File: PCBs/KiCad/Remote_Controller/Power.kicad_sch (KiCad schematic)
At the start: 24 parts, among them Q101 IRFML8244TRPBF, Q102 IRFML8244TRPBF, SW101 Power Switch, U101 AP63203WU, U102 LM74700, U103 MCP1700T-3002E/TT, U104 LM74700

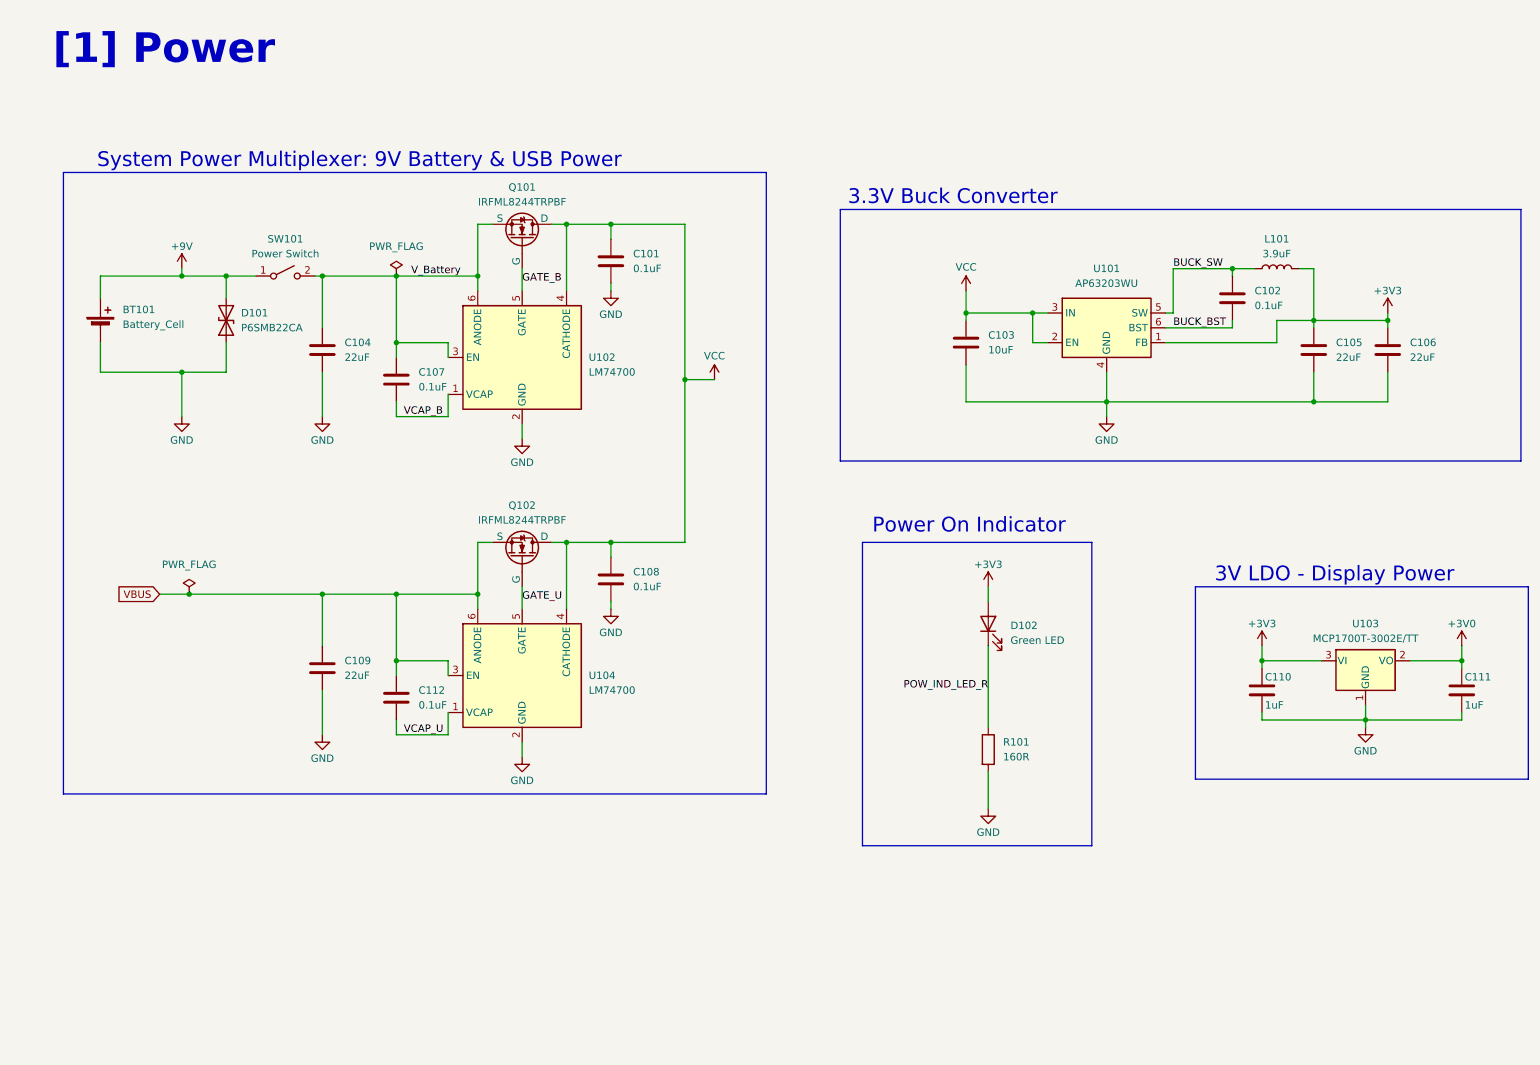
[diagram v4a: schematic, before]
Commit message: Add Latching Power On-Off switch circuit - allows user to turn device on and off with a tactile switch
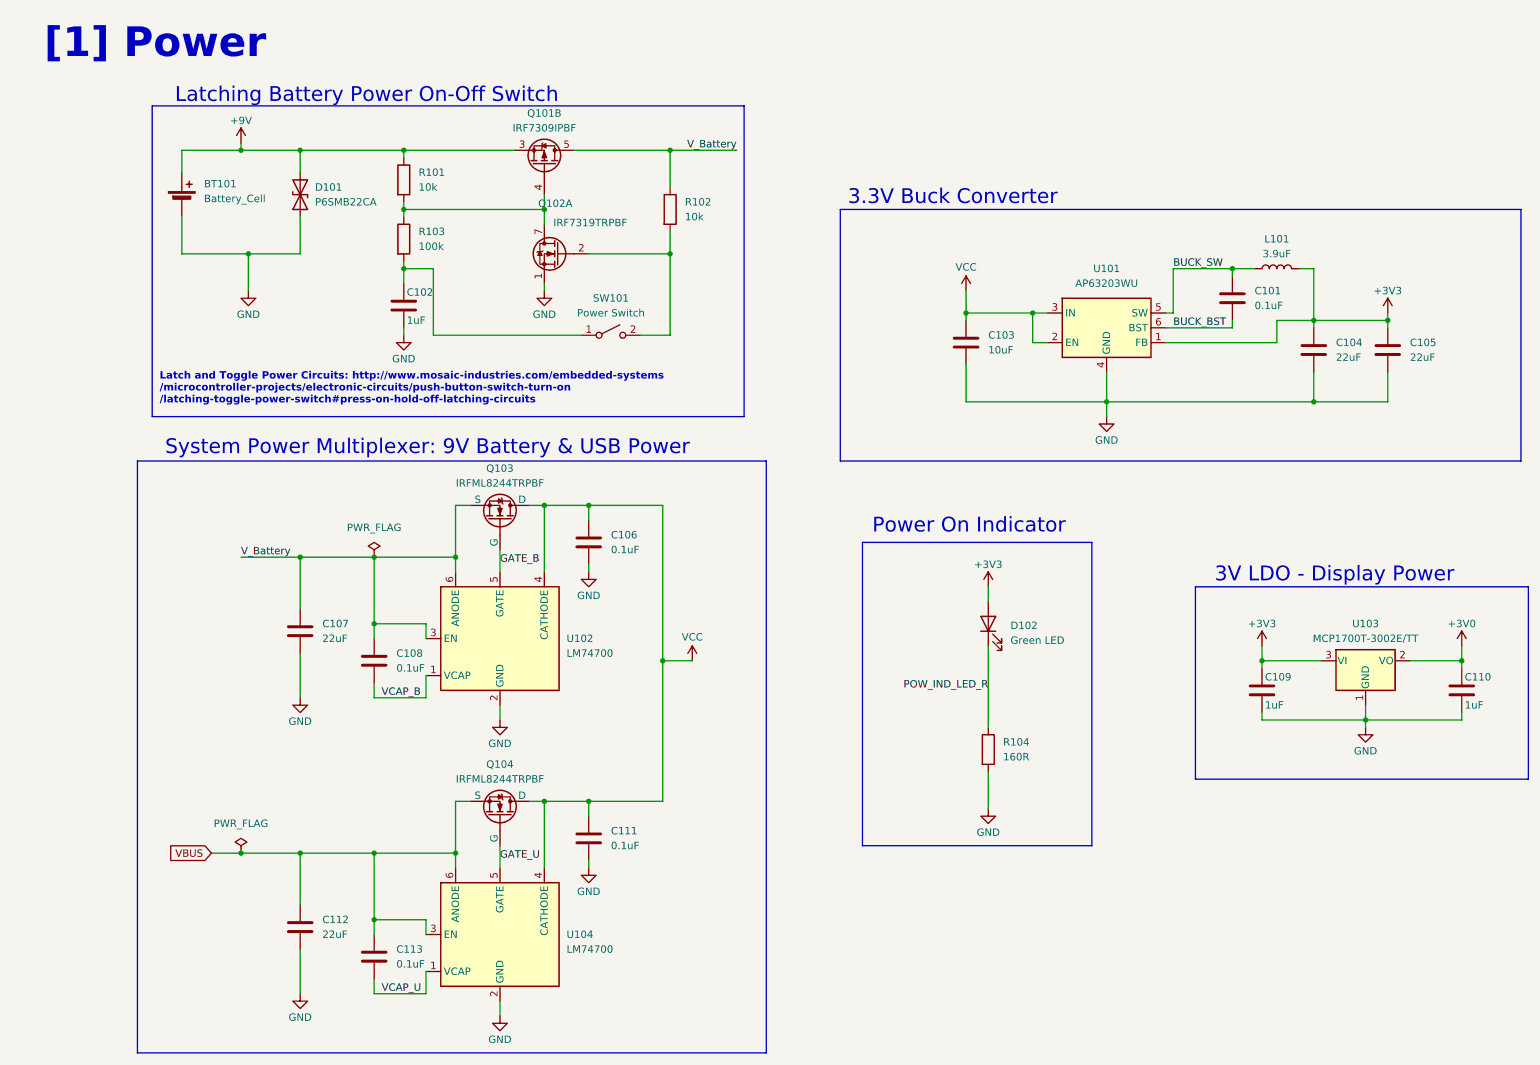
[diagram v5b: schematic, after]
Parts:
- added C102: 1uF, Capacitor_SMD:C_0402_1005Metric, symbol Device:C
- added Q101: IRF7309IPBF, Package_TO_SOT_THT:TO-220F-5_P3.4x2.06mm_StaggerEven_Lead1.86mm_Vertical, symbol Transistor_FET:IRF7309IPBF
- added Q102: IRF7319TRPBF, Package_TO_SOT_THT:TO-220F-5_P3.4x2.06mm_StaggerEven_Lead1.86mm_Vertical, symbol Transistor_FET:IRF7309IPBF
- added R101, R102: 10k, Resistor_SMD:R_0402_1005Metric, symbol Device:R
- added R103: 100k, Resistor_SMD:R_0603_1608Metric, symbol Device:R
- SW101: footprint (none) -> Button_Switch_SMD:SW_Push_1P1T_NO_CK_PTS125Sx43PSMTR
- renumbered C102 to C101, C105 to C104, C106 to C105, C101 to C106, C104 to C107, C107 to C108, C110 to C109, C111 to C110, C108 to C111, C109 to C112, C112 to C113, Q101 to Q103, Q102 to Q104, R101 to R104
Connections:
- net +9V: now also Q101.3 (1), R101.1; no longer SW101.1 (A)
- net GND: now also C102.2, Q102.1 (S)
- net V_Battery: now also Q101.5 (D), Q101.6 (D), R102.1; no longer SW101.2 (B)
- new net: Q102.2 (G), R102.2, SW101.2 (B)
- new net: C102.1, R103.2, SW101.1 (A)
- new net: Q101.4 (G), Q102.7 (D), Q102.8 (D), R101.2, R103.1
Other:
- note added: "Latch and Toggle Power Circuits: http://www.mosaic-industries.com/embedded-systems /microcontroller-projects/electronic-circuits/push-button-switch-turn-on /latching-toggle-power-switch#press-on-hold-off-latching-circuits"
- note added: "Latching Battery Power On-Off Switch"
- moved on the sheet: C106, C107, C108, C111, C112, C113, Q103, Q104, U102, U104

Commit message: Add Joystick footprint and passed ERC
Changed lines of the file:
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@@
 	)
 	(junction
+		(at 181.61 67.31)
+		(diameter 0)
+		(color 0 0 0 0)
+	)
+	(junction
 		(at 246.38 68.58)
 		(diameter 0)
@@
 	)
 	(junction
+		(at 64.77 39.37)
+		(diameter 0)
+		(color 0 0 0 0)
+	)
+	(junction
 		(at 198.12 82.55)
 		(diameter 0)
@@
 	(wire
 		(pts
-			(xy 59.69 39.37) (xy 77.47 39.37)
+			(xy 59.69 39.37) (xy 64.77 39.37)
 		)
 		(stroke
@@
 	(wire
 		(pts
+			(xy 181.61 67.31) (xy 173.99 67.31)
+		)
+		(stroke
+			(width 0)
+			(type default)
+		)
+	)
+	(wire
+		(pts
 			(xy 177.8 114.3) (xy 177.8 116.84)
 		)
@@
 	(wire
 		(pts
-			(xy 185.42 67.31) (xy 173.99 67.31)
+			(xy 185.42 67.31) (xy 181.61 67.31)
 		)
 		(stroke
@@
 	(wire
 		(pts
+			(xy 64.77 39.37) (xy 77.47 39.37)
+		)
+		(stroke
+			(width 0)
+			(type default)
+		)
+	)
+	(wire
+		(pts
 			(xy 259.08 135.89) (xy 259.08 137.16)
 		)
@@
 	(symbol
 		(lib_id "power:PWR_FLAG")
+		(at 181.61 67.31 0)
+		(unit 1)
+		(exclude_from_sim no)
+		(in_bom yes)
+		(on_board yes)
+		(dnp no)
+		(fields_autoplaced yes)
+		(property "Reference" "#FLG0104"
+			(at 181.61 65.405 0)
+			(effects
+				(font
+					(size 1.27 1.27)
+				)
+				(hide yes)
+			)
+		)
+		(property "Value" "PWR_FLAG"
+			(at 181.61 62.23 0)
+			(effects
+				(font
+					(size 1.27 1.27)
+				)
+			)
+		)
+		(property "Footprint" ""
+			(at 181.61 67.31 0)
+			(effects
+				(font
+					(size 1.27 1.27)
+				)
+				(hide yes)
+			)
+		)
+		(property "Datasheet" "~"
+			(at 181.61 67.31 0)
+			(effects
+				(font
+					(size 1.27 1.27)
+				)
+				(hide yes)
+			)
+		)
+		(property "Description" "Special symbol for telling ERC where power comes from"
+			(at 181.61 67.31 0)
+			(effects
+				(font
+					(size 1.27 1.27)
+				)
+				(hide yes)
+			)
+		)
+		(pin "1"
+		)
+		(instances
+			(project "Remote_Controller"
+				(path "/7afb5074-6b77-4607-a5eb-938c2def45ba/bc757f9b-317d-459c-8896-b31b23ed4983"
+					(reference "#FLG0104")
+					(unit 1)
+				)
+			)
+		)
+	)
+	(symbol
+		(lib_id "power:PWR_FLAG")
 		(at 72.39 109.22 0)
 		(unit 1)
@@
 					(unit 1)
 				)
+			)
+		)
+	)
+	(symbol
+		(lib_id "power:PWR_FLAG")
+		(at 64.77 39.37 0)
+		(unit 1)
+		(exclude_from_sim no)
+		(in_bom yes)
+		(on_board yes)
+		(dnp no)
+		(fields_autoplaced yes)
+		(property "Reference" "#FLG0103"
+			(at 64.77 37.465 0)
+			(effects
+				(font
+					(size 1.27 1.27)
+				)
+				(hide yes)
+			)
+		)
+		(property "Value" "PWR_FLAG"
+			(at 64.77 34.29 0)
+			(effects
+				(font
+					(size 1.27 1.27)
+				)
+			)
+		)
+		(property "Footprint" ""
+			(at 64.77 39.37 0)
+			(effects
+				(font
+					(size 1.27 1.27)
+				)
+				(hide yes)
+			)
+		)
+		(property "Datasheet" "~"
+			(at 64.77 39.37 0)
+			(effects
+				(font
+					(size 1.27 1.27)
+				)
+				(hide yes)
+			)
+		)
+		(property "Description" "Special symbol for telling ERC where power comes from"
+			(at 64.77 39.37 0)
+			(effects
+				(font
+					(size 1.27 1.27)
+				)
+				(hide yes)
+			)
+		)
+		(pin "1"
+		)
+		(instances
+			(project "Remote_Controller"
+				(path "/7afb5074-6b77-4607-a5eb-938c2def45ba/bc757f9b-317d-459c-8896-b31b23ed4983"
+					(reference "#FLG0103")
+					(unit 1)
+				)

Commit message: Updated joystick symbol, correct Dual fet footprint and annotated news in power toggle circuit
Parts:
- removed Q102: IRF7319TRPBF, Package_TO_SOT_THT:TO-220F-5_P3.4x2.06mm_StaggerEven_Lead1.86mm_Vertical, symbol Transistor_FET:IRF7309IPBF
- added unit 1 of Q101
- Q101: value IRF7309IPBF -> IRF7319; footprint Package_TO_SOT_THT:TO-220F-5_P3.4x2.06mm_StaggerEven_Lead1.86mm_Vertical -> Package_SO:SOIC-8_3.9x4.9mm_P1.27mm
- renumbered Q103 to Q102, Q104 to Q103
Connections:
- net GND: now also Q101.7 (D), Q101.8 (D)
- net PW_SW_R: now reaches R102.2, SW101.2 (B)
- net PW_SW_R: now also Q101.2 (G)
- net PWR_SW_CAP: now reaches C102.1, R103.2, SW101.1 (A)
- net PW_SW_R_G_S: now reaches Q101.4 (G), R101.2, R103.1
- net PW_SW_R_G_S: now also Q101.1 (S)
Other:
- note added: "Using symbol- IRF7309IPBF"
